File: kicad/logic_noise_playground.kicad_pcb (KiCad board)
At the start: 2 copper layers, 200 x 100 mm, 161 parts, among them J1 JACK_TRS_6PINS, P1 CONN_02X03, P10 CONN_01X03, P11 CONN_01X05, P12 CONN_02X04, P13 CONN_01X03, P14 CONN_01X02, P15 CONN_02X08, P16 CONN_01X04, P17 CONN_02X04, P18 CONN_01X04, P19 CONN_01X02, P2 CONN_01X02, P20 CONN_01X06, P21 CONN_02X03, P22 CONN_02X03, P23 CONN_01X02, P24 CONN_02X01, P25 CONN_01X02, P26 CONN_02X12, P27 CONN_01X02, P28 CONN_01X02, P29 CONN_01X02, P3 CONN_02X02, P30 CONN_01X02, P31 CONN_01X02, P32 CONN_01X03, P33 CONN_01X04, P34 CONN_01X04, P35 CONN_01X04, P36 CONN_01X04, P37 CONN_02X01, P38 CONN_01X04, P39 CONN_01X04, P4 CONN_02X06, P40 CONN_01X02, P5 CONN_02X02, P6 4017 Outs, P7 CONN_01X08, P8 CONN_02X03, P9 CONN_01X08, Q1 LM3904, SW1 Set, SW2 Clear, U1 40106, U2 4070, U3 40106, U4 4069, U5 4051, U6 4015, U7 4017, U8 4040

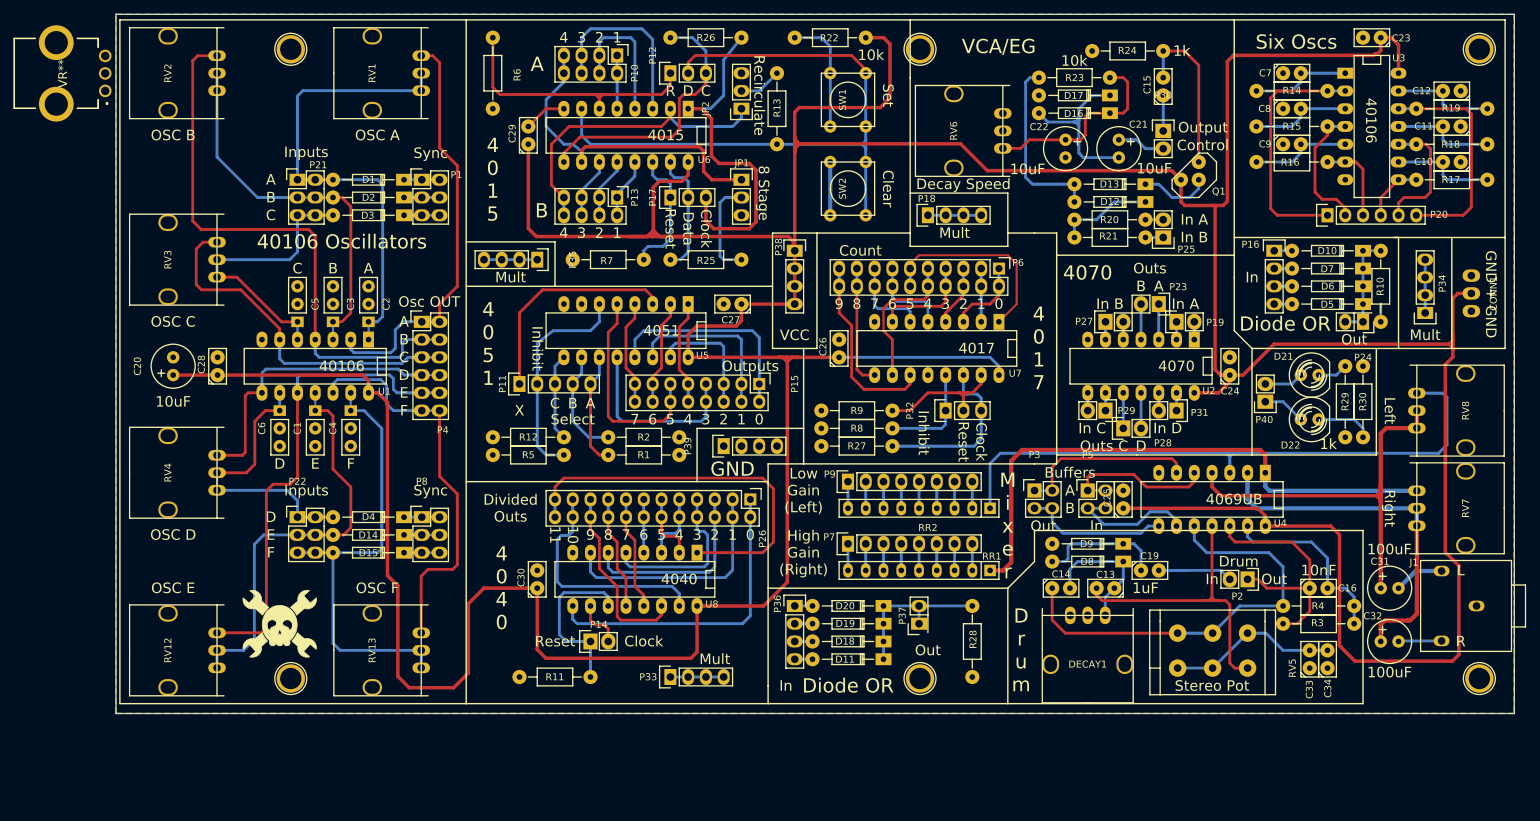
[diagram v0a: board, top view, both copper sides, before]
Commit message: change pots
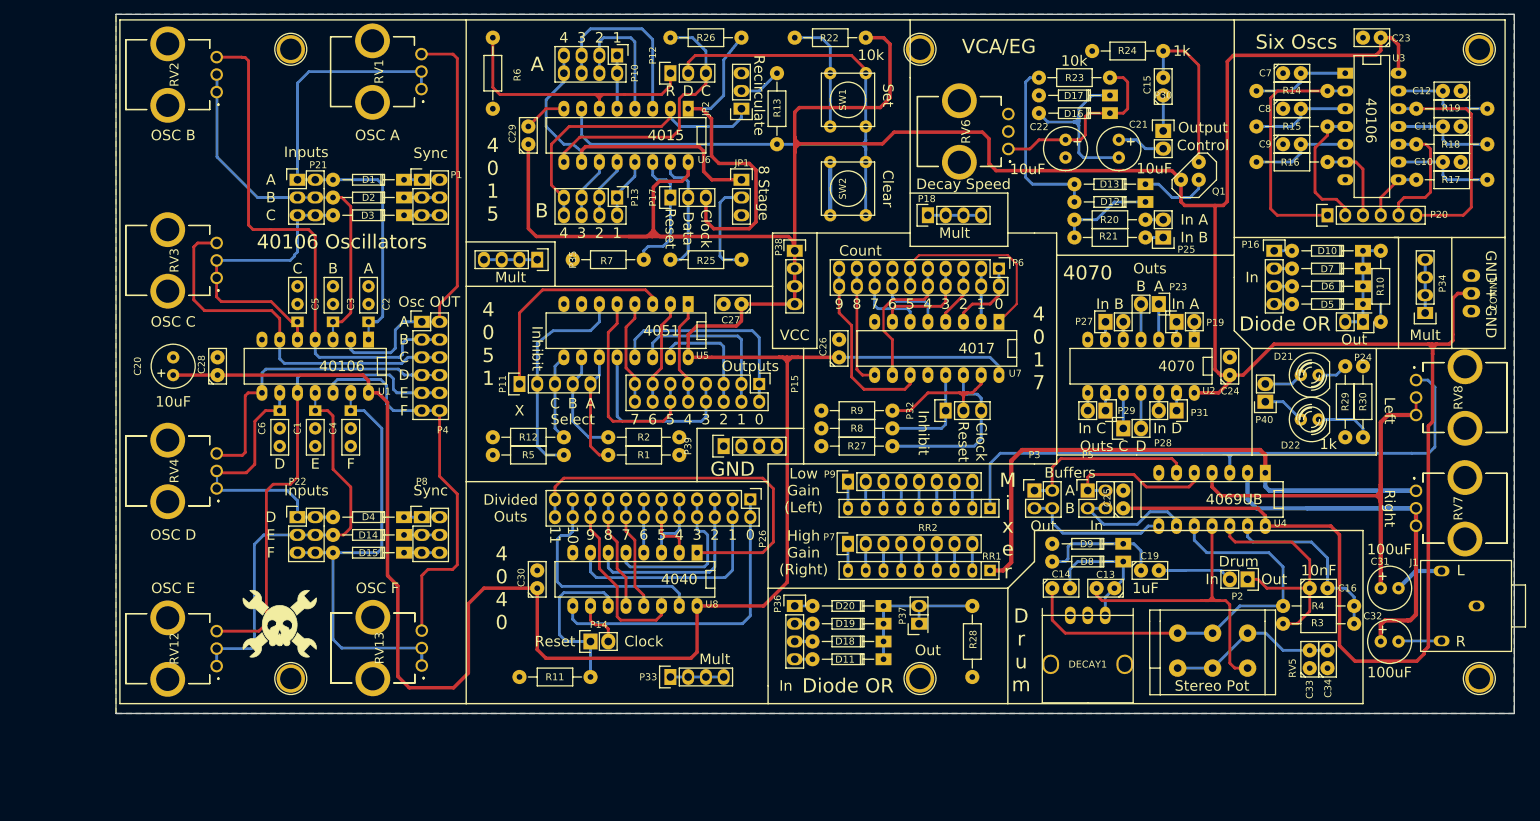
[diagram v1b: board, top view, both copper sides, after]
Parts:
- removed VR**: PTV09A4025FB104, logic_noise:PTV09A4025FB104
- RV1, RV12, RV13, RV2, RV3, RV4, RV6, RV7, RV8: footprint elliot:Potentiometer_9mm_vertical_pcb_mount -> logic_noise:PTV09A4025FB104
- moved RV8 6.72 mm to (220.9, 102.3)
- moved RV6 6.34 mm to (162.6, 69.3)
- moved RV7 5.70 mm to (220.9, 118.2)
- moved RV2 5.64 mm to (49.4, 61.1)
- moved RV3 5.60 mm to (49.4, 87.7)
- moved RV13 5.52 mm to (78.7, 143.1)
- moved RV1 5.52 mm to (78.7, 60.7)
- moved RV12 5.44 mm to (49.4, 143.2)
- moved RV4 5.43 mm to (49.4, 117.8)
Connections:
- U7 pad 12: (no net) -> unconnected-(U7-Cout-Pad12)
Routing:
- net /bass_drum/Buffer_A_In: track 81.7 -> 102.7 mm
- net /bass_drum/Buffer_A_Out: track 51.8 -> 67.4 mm
- net /40106_oscillators/OutB: track 81.9 -> 75.2 mm
- net /40106_oscillators/OutC: track 50.8 -> 53.7 mm
- net VCC: track 705.0 -> 702.5 mm
- net /40106_oscillators/InA: track 70.0 -> 72.2 mm
- net /40106_oscillators/OutA: track 59.9 -> 61.8 mm
- net /40106_oscillators/InC: track 41.5 -> 43.3 mm
- net /bass_drum/Buffer_B_Out: track 59.7 -> 61.3 mm
- net /bass_drum/Buffer_B_In: track 89.5 -> 88.0 mm
- net Net-(D16-K): track 28.4 -> 27.6 mm

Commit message: update resistors values
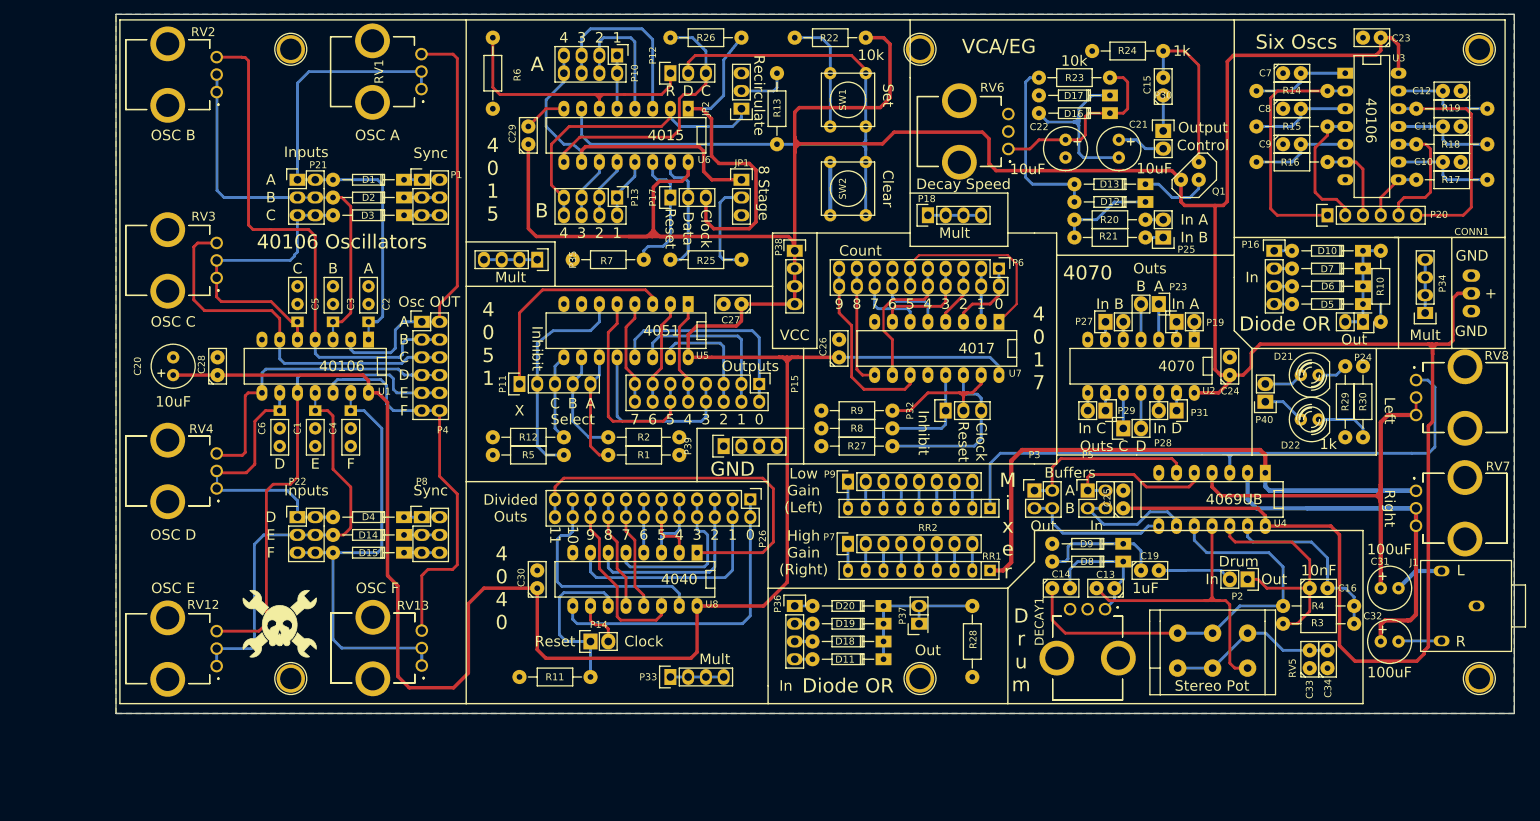
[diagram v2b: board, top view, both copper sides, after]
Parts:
- DECAY1: footprint elliot:Potentiometer_9mm_vertical_pcb_mount -> logic_noise:PTV09A4025FB104
- moved DECAY1 6.39 mm to (176.5, 135.1)
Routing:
- net /40106_oscillators/InB: track 54.9 -> 57.7 mm
- net Net-(JP2-Pad2): track 6.13 -> 7.34 mm
- net VCC: track 702.5 -> 703.7 mm
- net Net-(D8-K): track 19.6 -> 18.7 mm
- net Net-(C13-Pad2): track 45.4 -> 44.8 mm

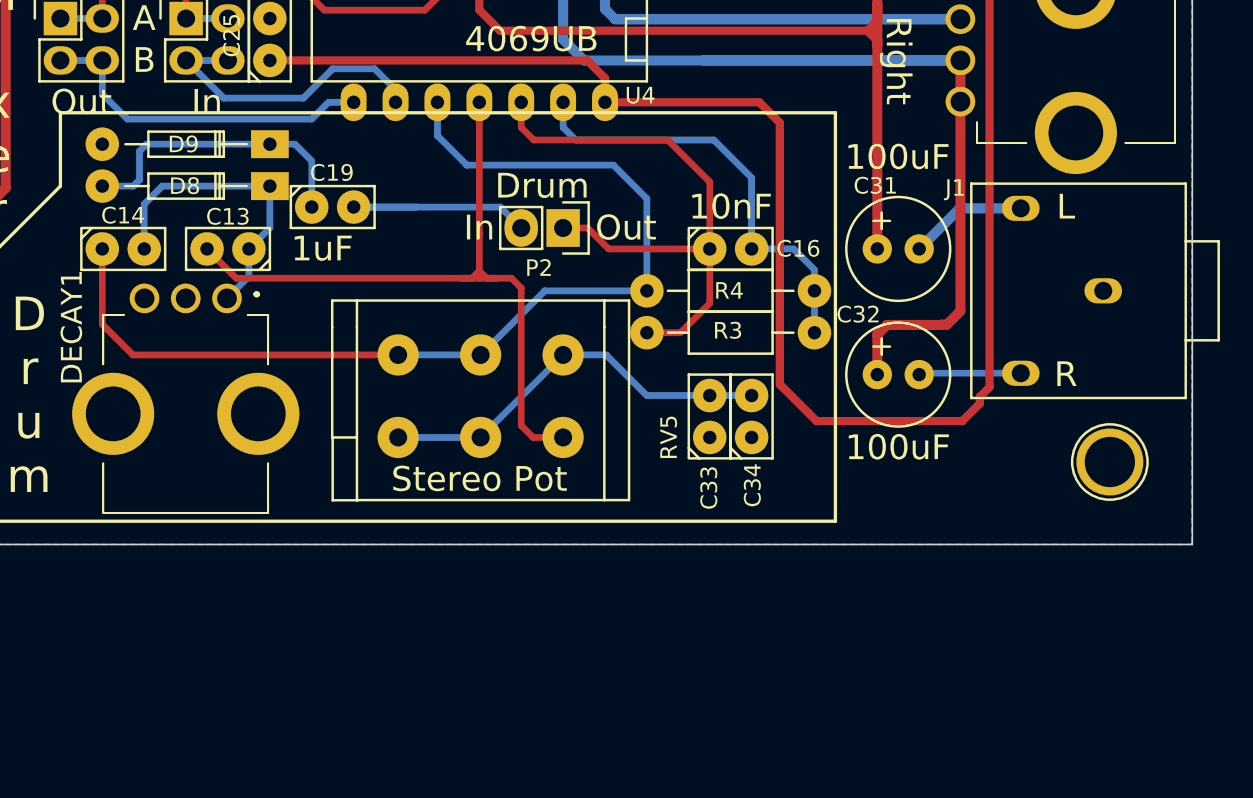
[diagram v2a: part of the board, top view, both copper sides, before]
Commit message: update stereo TRSS connector
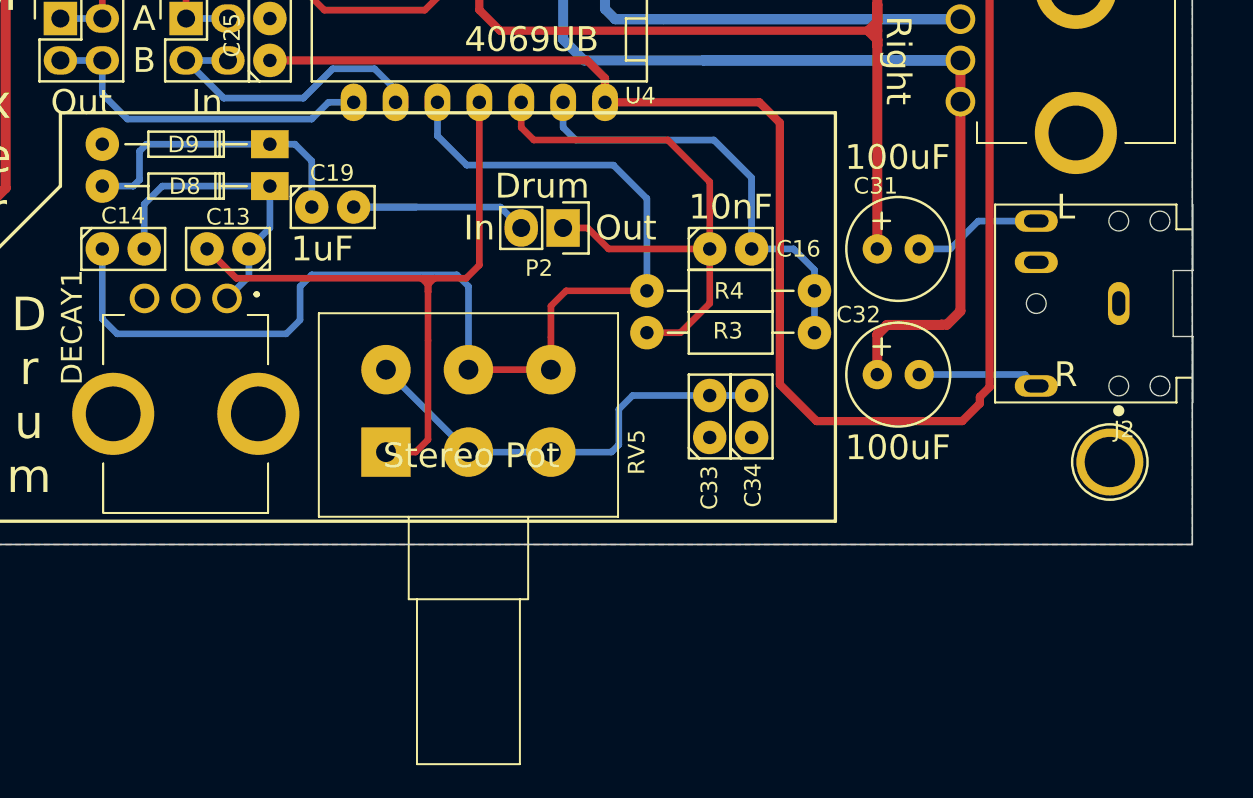
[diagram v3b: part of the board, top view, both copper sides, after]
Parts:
- removed J1: JACK_TRS_6PINS, elliot:stereo_jack
- added J2: SJ1-3524NG, logic_noise:CUI_SJ1-3524NG, F.Cu at (230.5, 135.4)
- RV5: footprint Potentiometers:Potentiometer_Alps-RK16-double -> Potentiometer_THT:Potentiometer_Alps_RK163_Dual_Horizontal
- moved RV5 10.8 mm to (186.1, 144.4), turned to 90 degrees
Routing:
- net Net-(C14-Pad1): track 61.4 -> 71.8 mm
- net Net-(C13-Pad2): track 44.8 -> 41.7 mm
- net Net-(C32-Pad2): track 6.19 -> 7.39 mm
- net Net-(C33-Pad2): track 25.7 -> 26.9 mm
- net Net-(C31-Pad2): track 7.18 -> 7.80 mm
